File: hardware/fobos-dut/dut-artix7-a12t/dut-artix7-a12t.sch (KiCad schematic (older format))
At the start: 4 parts

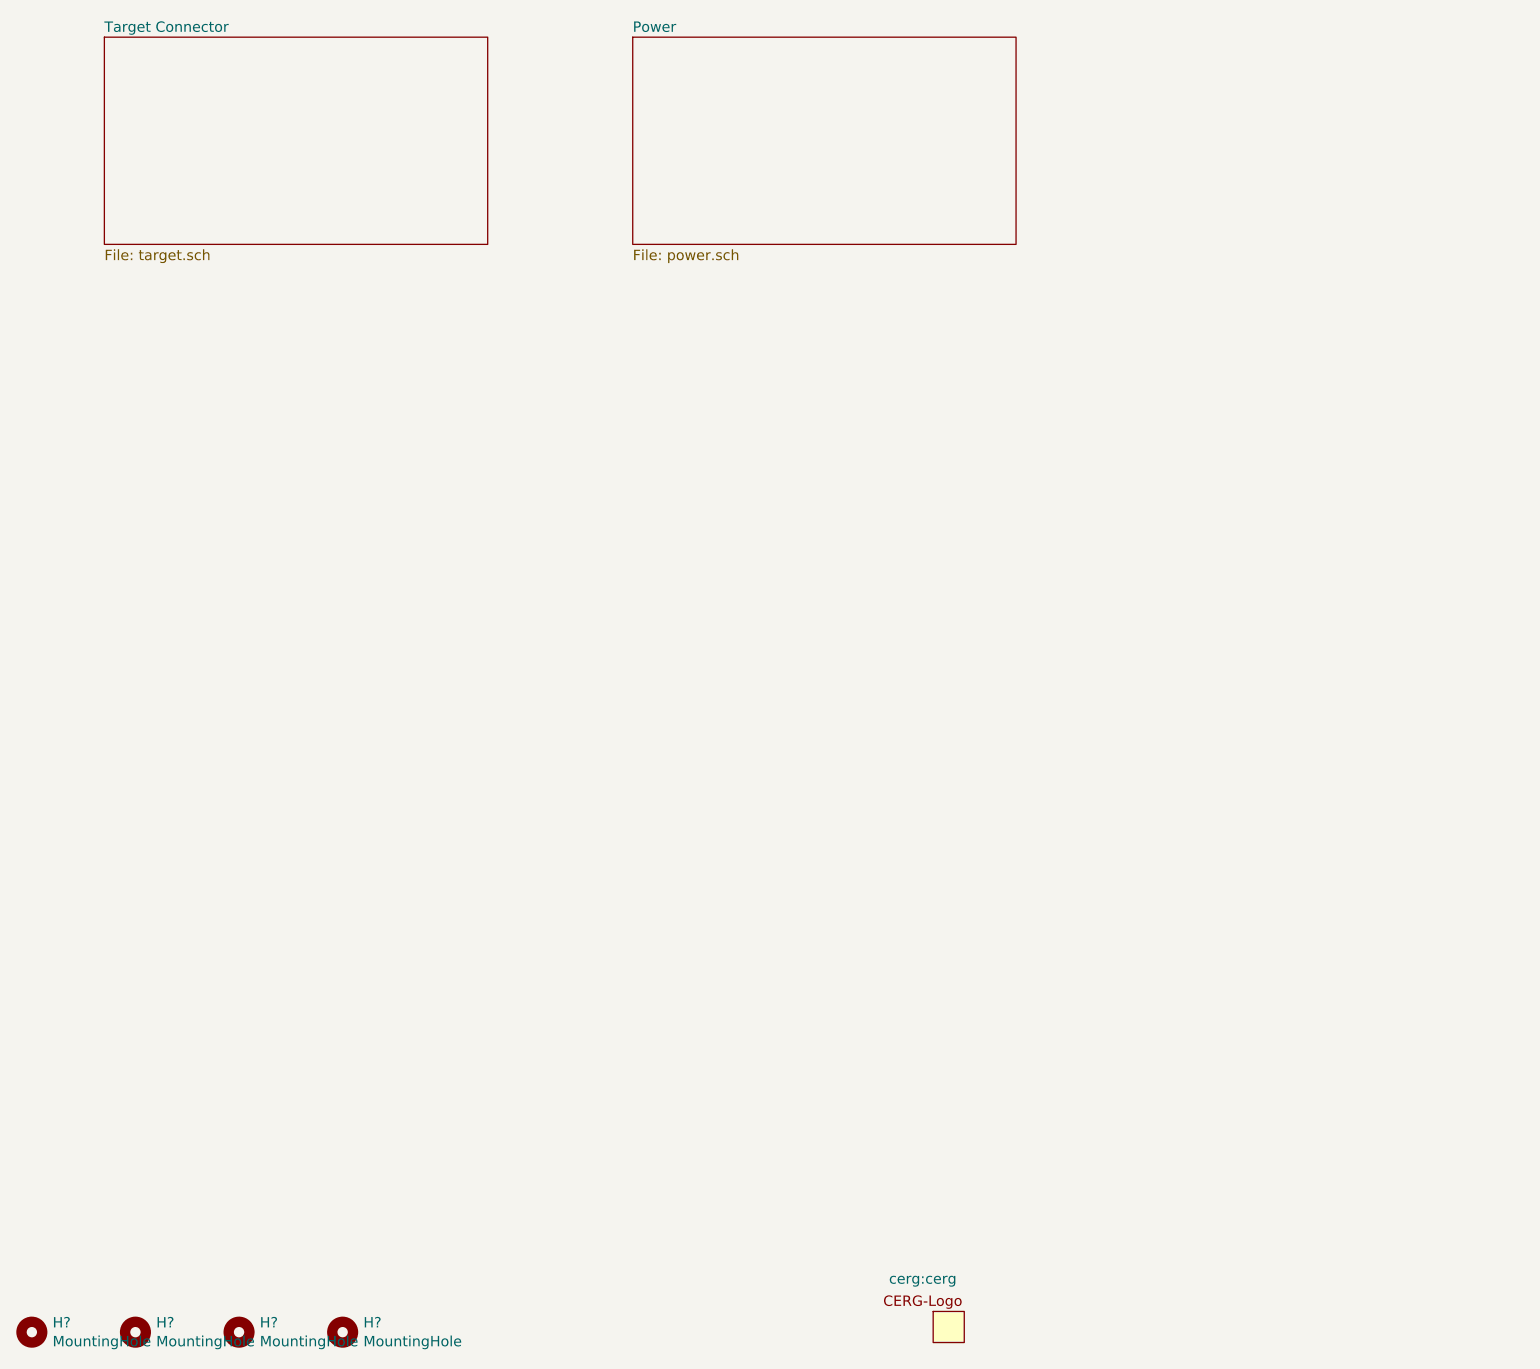
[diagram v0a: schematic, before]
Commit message: started adding FPGA to Artix7 DUT
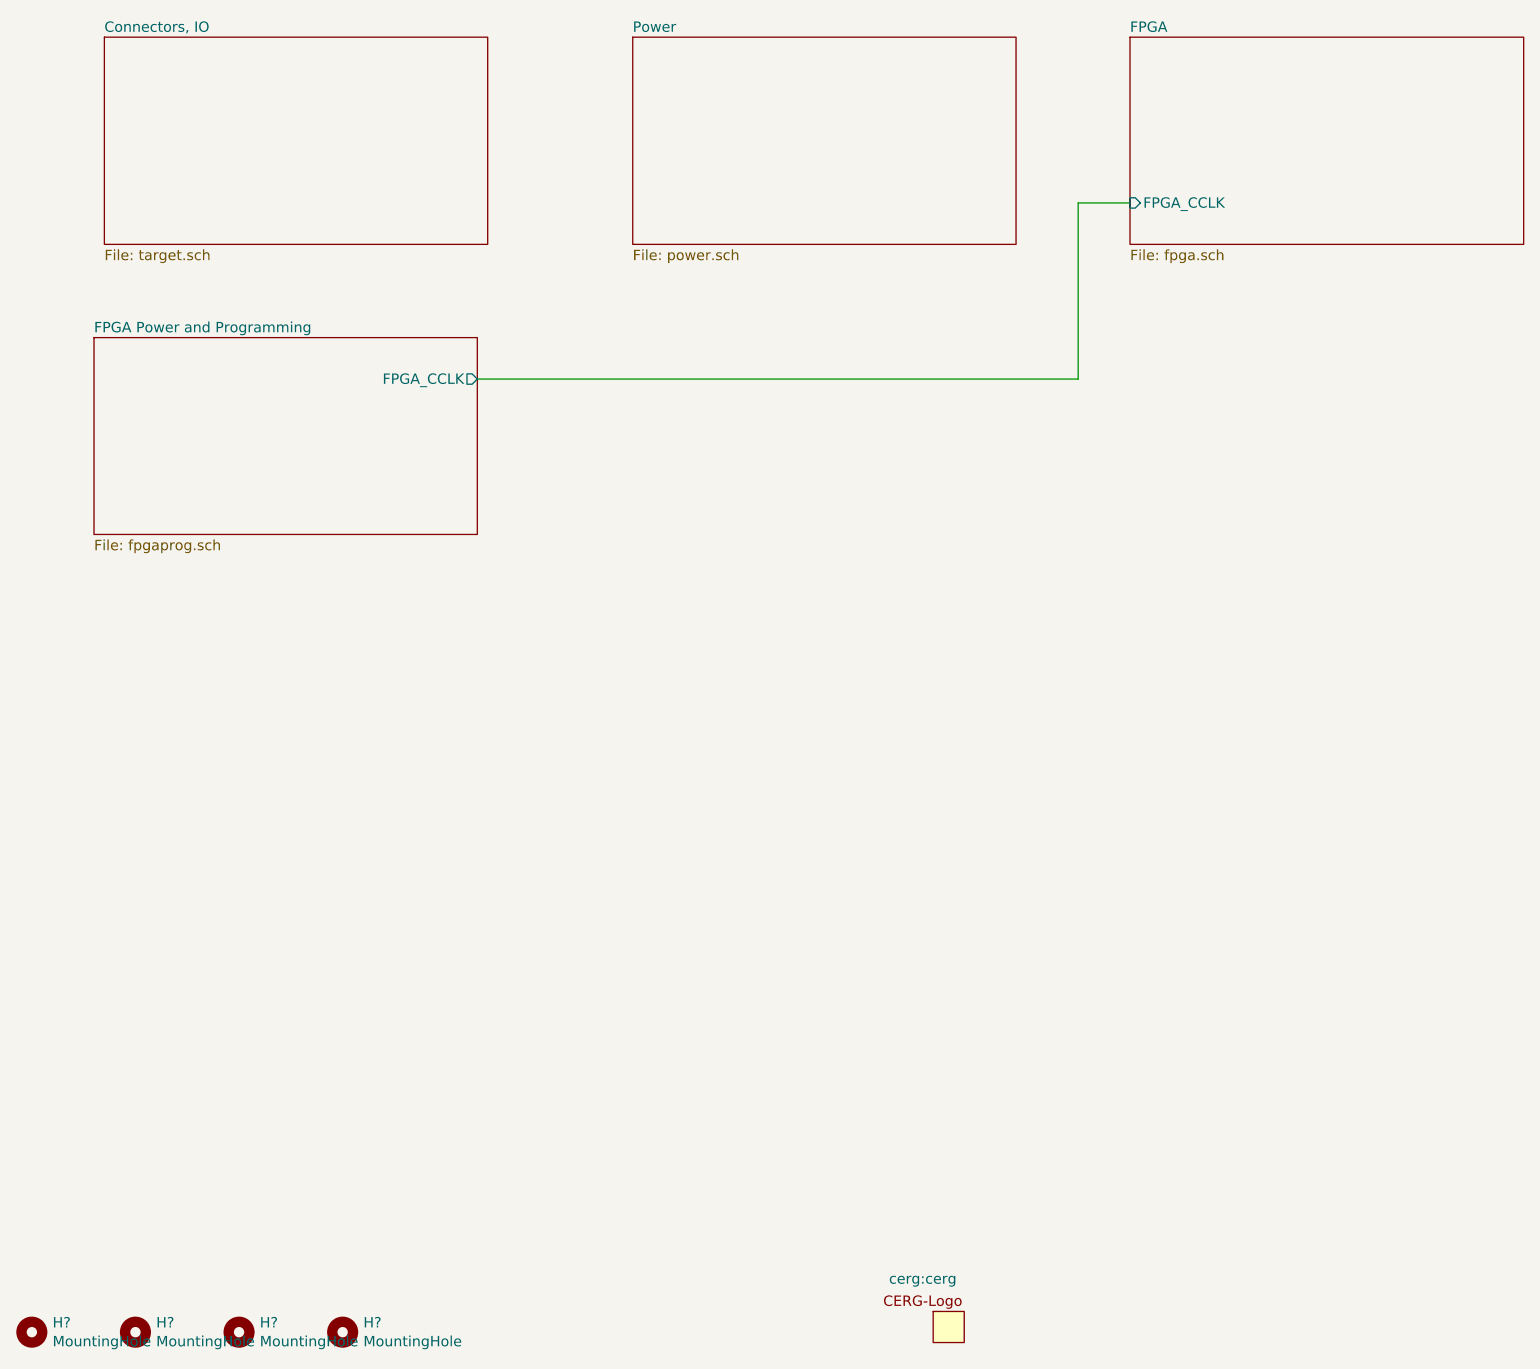
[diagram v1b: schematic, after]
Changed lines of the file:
@@
 $Descr USLetter 11000 8500
 encoding utf-8
-Sheet 1 3
+Sheet 1 5
 Title "FOBOS Artix-7 a12t DUT"
 Date "2020-07-28"
@@
 S 1600 1200 1850 1000
 U 5F20DA36
-F0 "Target Connector" 50
+F0 "Connectors, IO" 50
 F1 "target.sch" 50
 $EndSheet
@@
 F1 "power.sch" 50
 $EndSheet
+$Sheet
+S 6550 1200 1900 1000
+U 5F22D594
+F0 "FPGA" 50
+F1 "fpga.sch" 50
+F2 "FPGA_CCLK" I L 6550 2000 50
+$EndSheet
+$Sheet
+S 1550 2650 1850 950
+U 5F3A1954
+F0 "FPGA Power and Programming" 50
+F1 "fpgaprog.sch" 50
+F2 "FPGA_CCLK" O R 3400 2850 50
+$EndSheet
+Wire Wire Line
+	3400 2850 6300 2850
+Wire Wire Line
+	6300 2850 6300 2000
+Wire Wire Line
+	6300 2000 6550 2000
 $EndSCHEMATC

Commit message: artix 7 dut PCB work
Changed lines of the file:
@@
 $EndComp
 $Sheet
-S 1600 1200 1850 1000
+S 1550 1200 1850 1000
 U 5F20DA36
 F0 "Connectors, IO" 50
@@
 $EndSheet
 $Sheet
-S 4150 1200 1850 1000
+S 4100 1200 1850 1000
 U 5F449901
 F0 "Power" 50
@@
 $EndSheet
 $Sheet
-S 6550 1200 1900 1000
+S 4100 2650 1850 1000
 U 5F22D594
 F0 "FPGA" 50
 F1 "fpga.sch" 50
-F2 "FPGA_CCLK" I L 6550 2000 50
+F2 "FPGA_CCLK" I L 4100 2850 50
 $EndSheet
 $Sheet
-S 1550 2650 1850 950
+S 1550 2650 1850 1000
 U 5F3A1954
 F0 "FPGA Power and Programming" 50
@@
 $EndSheet
 Wire Wire Line
-	3400 2850 6300 2850
-Wire Wire Line
-	6300 2850 6300 2000
-Wire Wire Line
-	6300 2000 6550 2000
+	3400 2850 4100 2850
 $EndSCHEMATC

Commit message: artix 7 dut updates
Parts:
- gave numbers to parts that had none: 4
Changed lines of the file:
@@
 $EndBitmap
 $Comp
-L Mechanical:MountingHole H?
+L Mechanical:MountingHole H1
 U 1 1 5F20C988
 P 1250 7450
-F 0 "H?" H 1350 7496 50  0000 L CNN
+F 0 "H1" H 1350 7496 50  0000 L CNN
 F 1 "MountingHole" H 1350 7405 50  0000 L CNN
 F 2 "" H 1250 7450 50  0001 C CNN
@@
 $EndComp
 $Comp
-L Mechanical:MountingHole H?
+L Mechanical:MountingHole H2
 U 1 1 5F20CFDF
 P 1750 7450
-F 0 "H?" H 1850 7496 50  0000 L CNN
+F 0 "H2" H 1850 7496 50  0000 L CNN
 F 1 "MountingHole" H 1850 7405 50  0000 L CNN
 F 2 "" H 1750 7450 50  0001 C CNN
@@
 $EndComp
 $Comp
-L Mechanical:MountingHole H?
+L Mechanical:MountingHole H3
 U 1 1 5F20D16B
 P 2250 7450
-F 0 "H?" H 2350 7496 50  0000 L CNN
+F 0 "H3" H 2350 7496 50  0000 L CNN
 F 1 "MountingHole" H 2350 7405 50  0000 L CNN
 F 2 "" H 2250 7450 50  0001 C CNN
@@
 $EndComp
 $Comp
-L Mechanical:MountingHole H?
+L Mechanical:MountingHole H4
 U 1 1 5F20D2F6
 P 2750 7450
-F 0 "H?" H 2850 7496 50  0000 L CNN
+F 0 "H4" H 2850 7496 50  0000 L CNN
 F 1 "MountingHole" H 2850 7405 50  0000 L CNN
 F 2 "" H 2750 7450 50  0001 C CNN
@@
 $EndComp
 $Comp
-L cerg:CERG-logo #LOGO?
+L cerg:CERG-logo #LOGO1
 U 1 1 5F20D55F
 P 5550 7350
-F 0 "#LOGO?" H 5550 7625 50  0001 C CNN
+F 0 "#LOGO1" H 5550 7625 50  0001 C CNN
 F 1 "CERG-logo" H 5550 7125 50  0001 C CNN
 F 2 "cerg:cerg" H 5550 7507 50  0000 C CNN

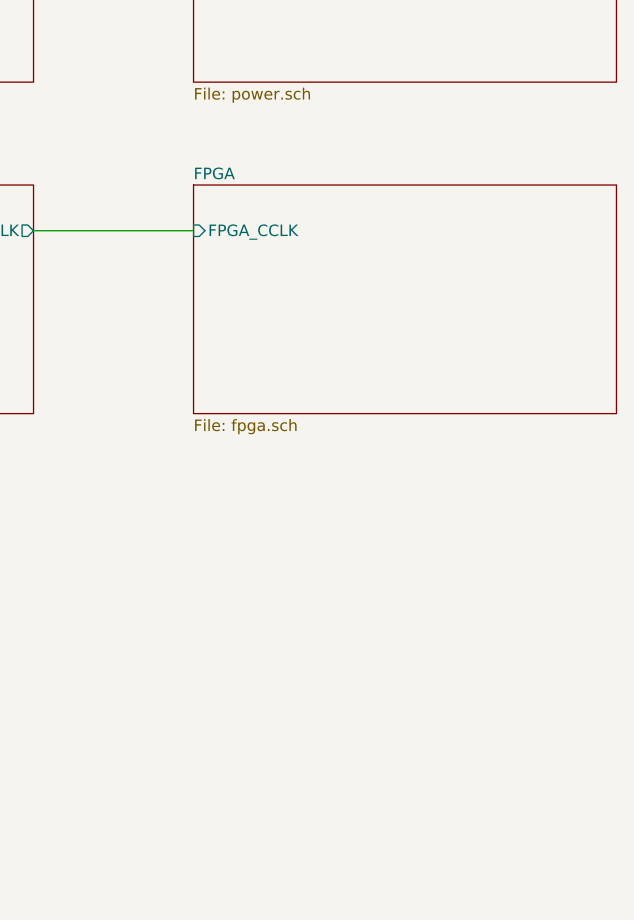
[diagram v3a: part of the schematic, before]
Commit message: -Added TS3A27518EIPWRQ1 6 circuit analog SPDT switch -Connected tripple output power supply to FPGA power pins -Added bypass and decoupling capacitors to the FPGA power pins(these will be DNP) -Swapped out the old bulky banana jack socket parts for 1050752001 and 1050753001 -Added JTAG header -Added test loops -Added boot mode dip switch -Swapped out the right angle 0.1" headers for vertical 0.1" headers(personal preference) -Working my way through the 7_series_schematic_review_recommendations spreadsheet
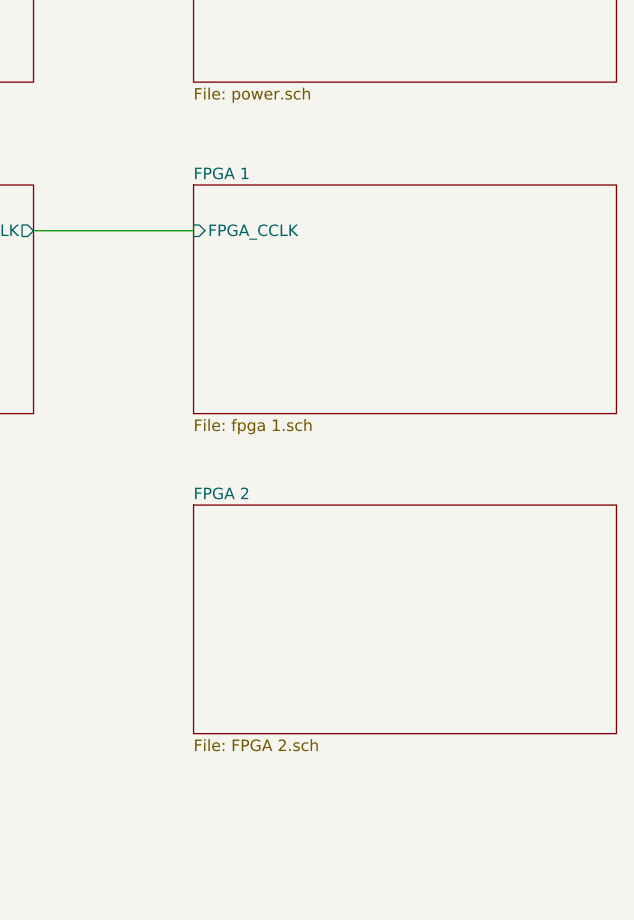
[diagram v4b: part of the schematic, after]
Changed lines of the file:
@@
 $Descr USLetter 11000 8500
 encoding utf-8
-Sheet 1 5
+Sheet 1 6
 Title "FOBOS Artix-7 a12t DUT"
 Date "2020-07-28"
@@
 S 4100 2650 1850 1000
 U 5F22D594
-F0 "FPGA" 50
-F1 "fpga.sch" 50
+F0 "FPGA 1" 50
+F1 "fpga 1.sch" 50
 F2 "FPGA_CCLK" I L 4100 2850 50
 $EndSheet
@@
 Wire Wire Line
 	3400 2850 4100 2850
+$Sheet
+S 4100 4050 1850 1000
+U 6004C151
+F0 "FPGA 2" 50
+F1 "FPGA 2.sch" 50
+$EndSheet
 $EndSCHEMATC

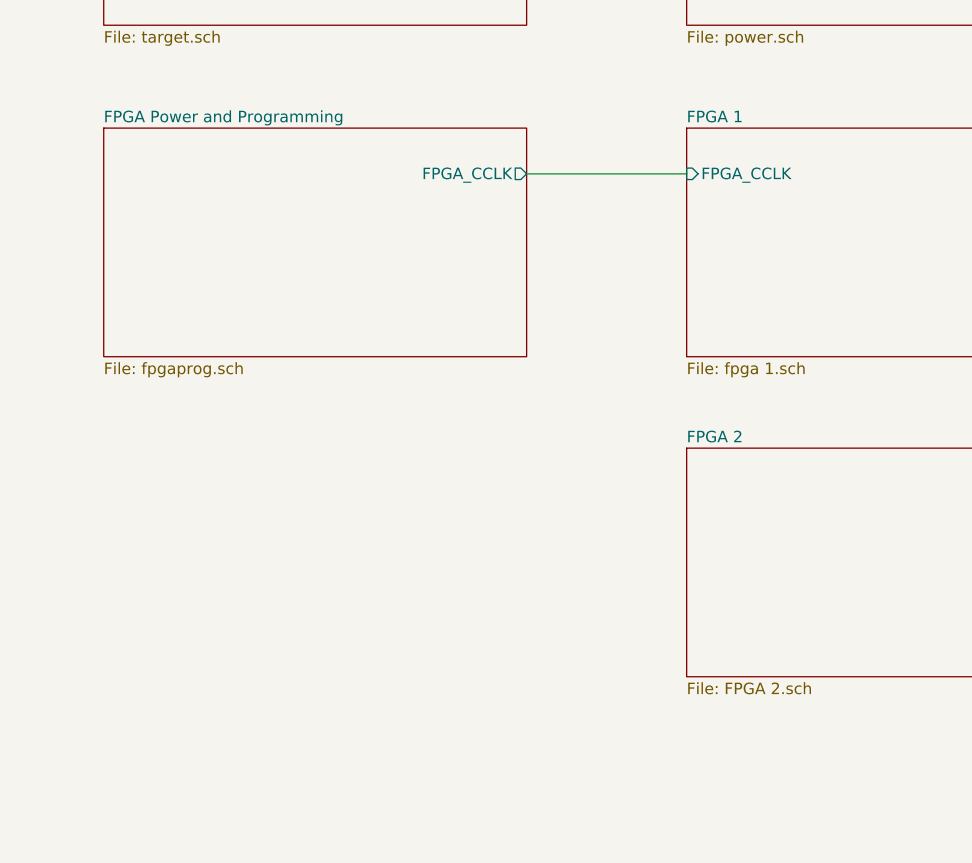
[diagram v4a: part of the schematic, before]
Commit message: Schematic is 99% complete, getting started on layout
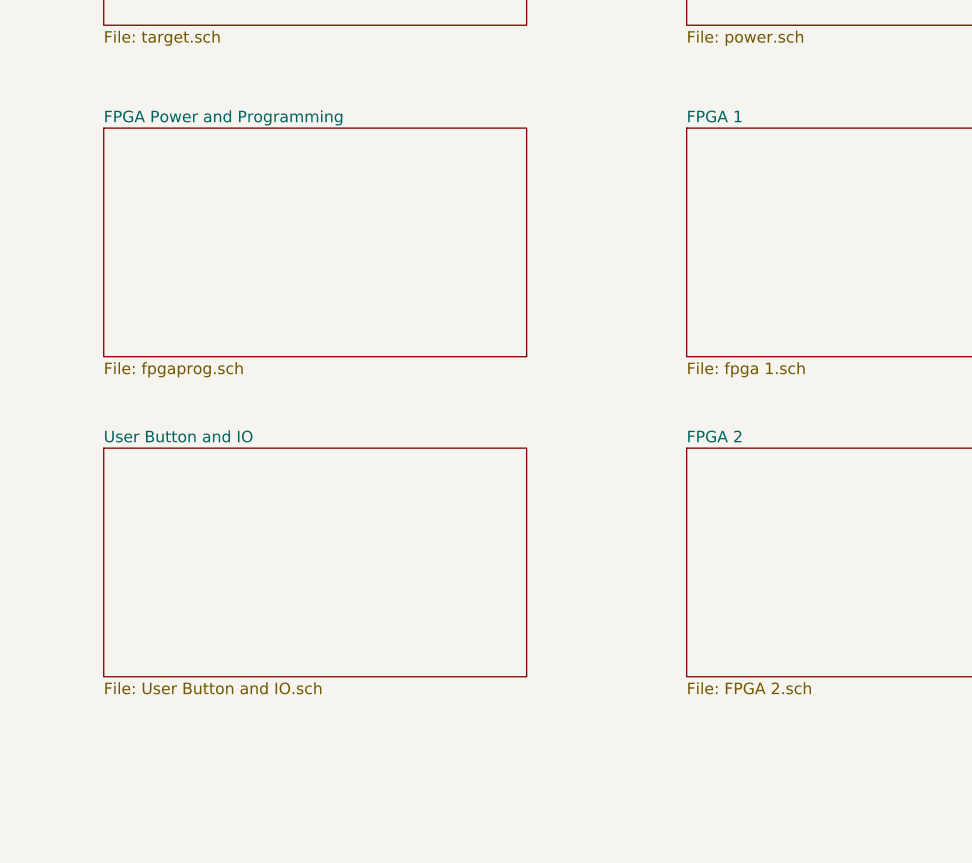
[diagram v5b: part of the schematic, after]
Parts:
- H1, H2, H3, H4: footprint (none) -> cerg:MH_4-40
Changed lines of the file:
@@
 $Descr USLetter 11000 8500
 encoding utf-8
-Sheet 1 6
+Sheet 1 7
 Title "FOBOS Artix-7 a12t DUT"
 Date "2020-07-28"
@@
 F 0 "H1" H 1350 7496 50  0000 L CNN
 F 1 "MountingHole" H 1350 7405 50  0000 L CNN
-F 2 "" H 1250 7450 50  0001 C CNN
+F 2 "cerg:MH_4-40" H 1250 7450 50  0001 C CNN
 F 3 "~" H 1250 7450 50  0001 C CNN
 	1    1250 7450
@@
 F 0 "H2" H 1850 7496 50  0000 L CNN
 F 1 "MountingHole" H 1850 7405 50  0000 L CNN
-F 2 "" H 1750 7450 50  0001 C CNN
+F 2 "cerg:MH_4-40" H 1750 7450 50  0001 C CNN
 F 3 "~" H 1750 7450 50  0001 C CNN
 	1    1750 7450
@@
 F 0 "H3" H 2350 7496 50  0000 L CNN
 F 1 "MountingHole" H 2350 7405 50  0000 L CNN
-F 2 "" H 2250 7450 50  0001 C CNN
+F 2 "cerg:MH_4-40" H 2250 7450 50  0001 C CNN
 F 3 "~" H 2250 7450 50  0001 C CNN
 	1    2250 7450
@@
 F 0 "H4" H 2850 7496 50  0000 L CNN
 F 1 "MountingHole" H 2850 7405 50  0000 L CNN
-F 2 "" H 2750 7450 50  0001 C CNN
+F 2 "cerg:MH_4-40" H 2750 7450 50  0001 C CNN
 F 3 "~" H 2750 7450 50  0001 C CNN
 	1    2750 7450
@@
 F0 "FPGA 1" 50
 F1 "fpga 1.sch" 50
-F2 "FPGA_CCLK" I L 4100 2850 50
 $EndSheet
 $Sheet
@@
 F0 "FPGA Power and Programming" 50
 F1 "fpgaprog.sch" 50
-F2 "FPGA_CCLK" O R 3400 2850 50
 $EndSheet
-Wire Wire Line
-	3400 2850 4100 2850
 $Sheet
 S 4100 4050 1850 1000
@@
 F1 "FPGA 2.sch" 50
 $EndSheet
+$Sheet
+S 1550 4050 1850 1000
+U 600CE672
+F0 "User Button and IO" 50
+F1 "User Button and IO.sch" 50
+$EndSheet
 $EndSCHEMATC
